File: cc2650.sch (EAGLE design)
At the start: 27 parts, among them IC1 TPS73133DBVR, IC4 CC2650MODAMOHR, SW1 SPST_TACT-KMR2, SW3 SPST_TACT-KMR2

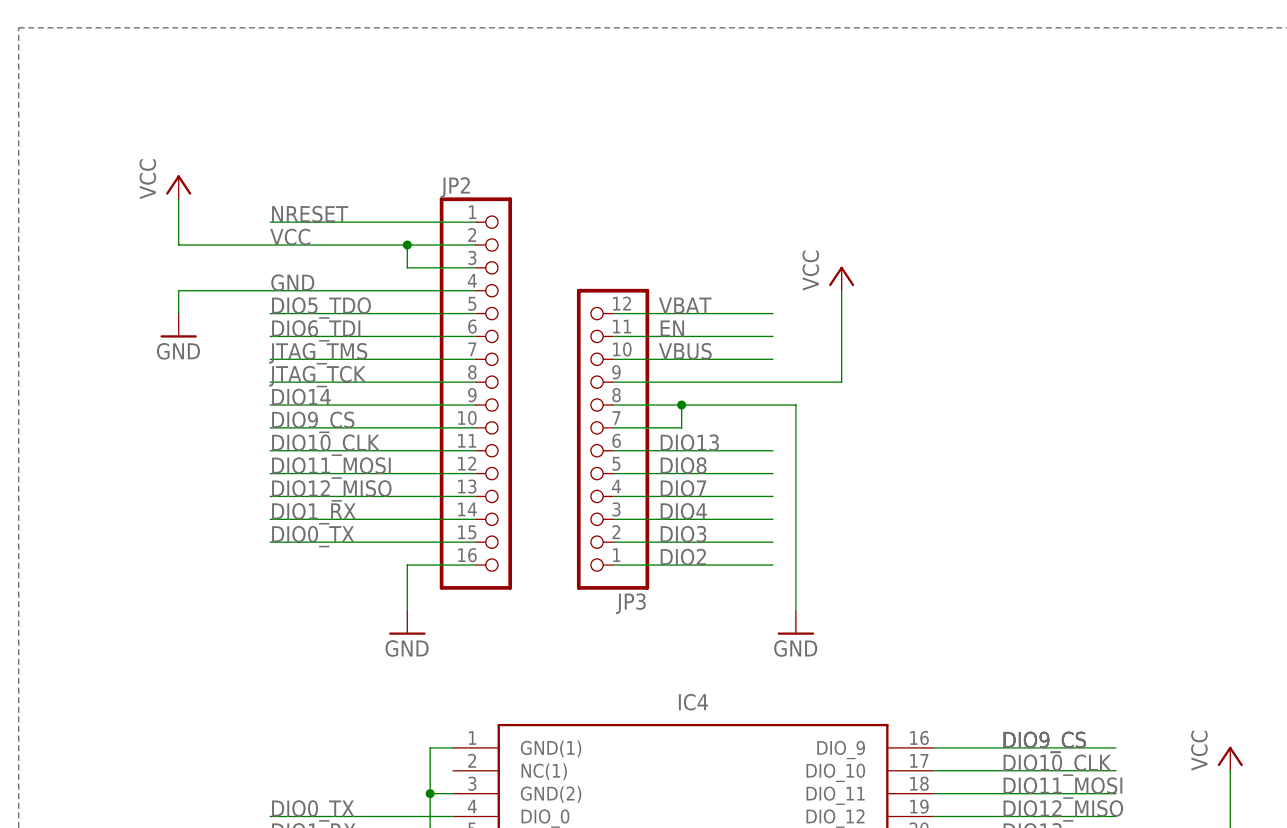
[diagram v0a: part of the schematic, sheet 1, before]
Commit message: modified adafruit FeatehrWing pin part to remove bottom left hole. Swapped modified FeatherWing for the 1x12 & 1x16 pin headers.
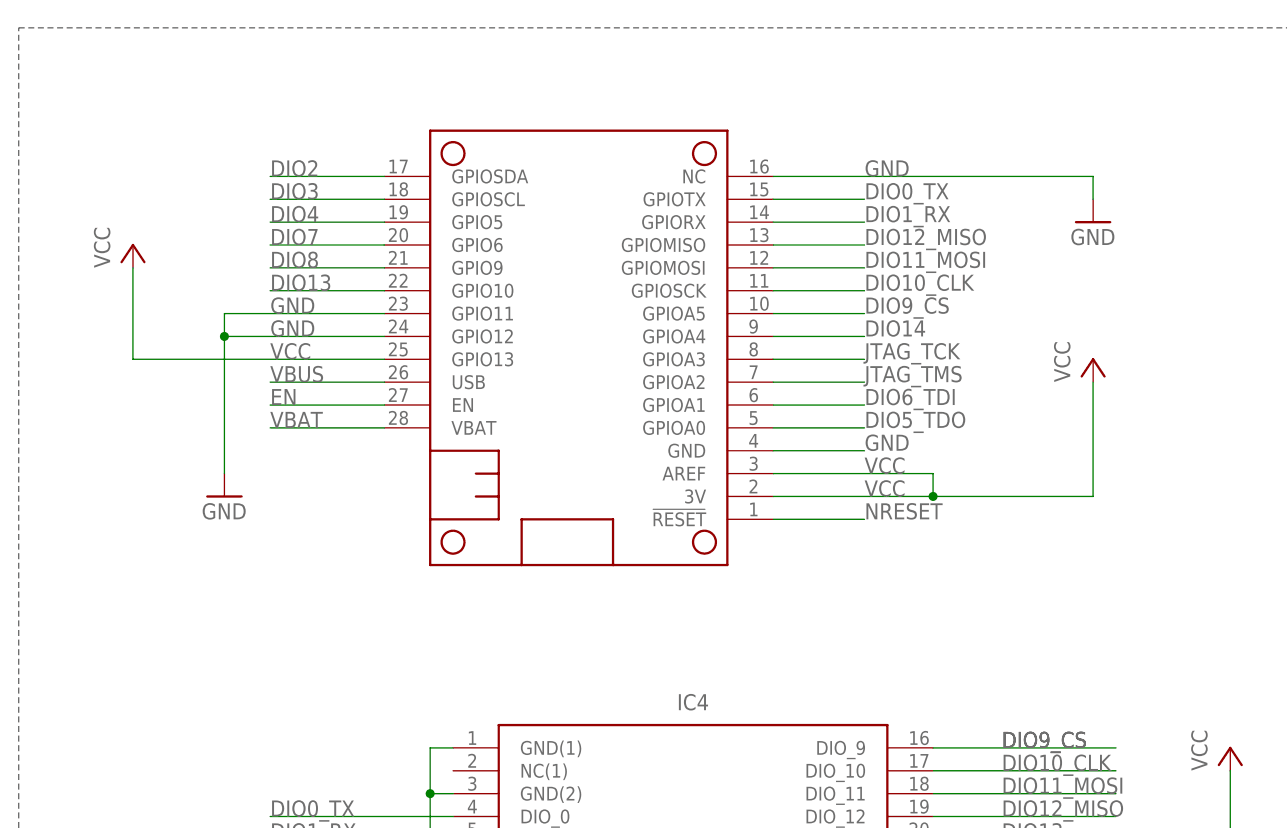
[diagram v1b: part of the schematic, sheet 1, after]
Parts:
- removed JP2: (no value), microbuilder:HEADER-1X16ROUND
- removed JP3: (no value), microbuilder:HEADER-1X12
- added MS1: FEATHERWING_NODIM, wing_modified:FEATHERWING_NODIM
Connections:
- net DIO0_TX: now also MS1.GPIOTX; no longer JP2.15
- net DIO10_CLK: now also MS1.GPIOSCK; no longer JP2.11
- net DIO11_MOSI: now also MS1.GPIOMOSI; no longer JP2.12
- net DIO12_MISO: now also MS1.GPIOMISO; no longer JP2.13
- net DIO13: now also MS1.GPIO10; no longer JP3.6
- net DIO14: now also MS1.GPIOA4; no longer JP2.9
- net DIO1_RX: now also MS1.GPIORX; no longer JP2.14
- net DIO2: now also MS1.GPIOSDA; no longer JP3.1
- net DIO3: now also MS1.GPIOSCL; no longer JP3.2
- net DIO4: now also MS1.GPIO5; no longer JP3.3
- net DIO5_TDO: now also MS1.GPIOA0; no longer JP2.5
- net DIO6_TDI: now also MS1.GPIOA1; no longer JP2.6
- net DIO7: now also MS1.GPIO6; no longer JP3.4
- net DIO8: now also MS1.GPIO9; no longer JP3.5
- net DIO9_CS: now also MS1.GPIOA5; no longer JP2.10
- net EN: now also MS1.EN; no longer JP3.11
- net GND: now also MS1.GND, MS1.GPIO11, MS1.GPIO12, MS1.NC; no longer JP2.16, JP2.4, JP3.7, JP3.8
- net JTAG_TCK: now also MS1.GPIOA3; no longer JP2.8
- net JTAG_TMS: now also MS1.GPIOA2; no longer JP2.7
- net NRESET: now also MS1.!RESET; no longer JP2.1
- net VBAT: now also MS1.VBAT; no longer JP3.12
- net VBUS: now also MS1.USB; no longer JP3.10
- net VCC: now also MS1.3V, MS1.AREF, MS1.GPIO13; no longer JP2.2, JP2.3, JP3.9
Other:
- note removed: "Mounting Holes: 125 mil for 4-40/M2.5/M3 screws"

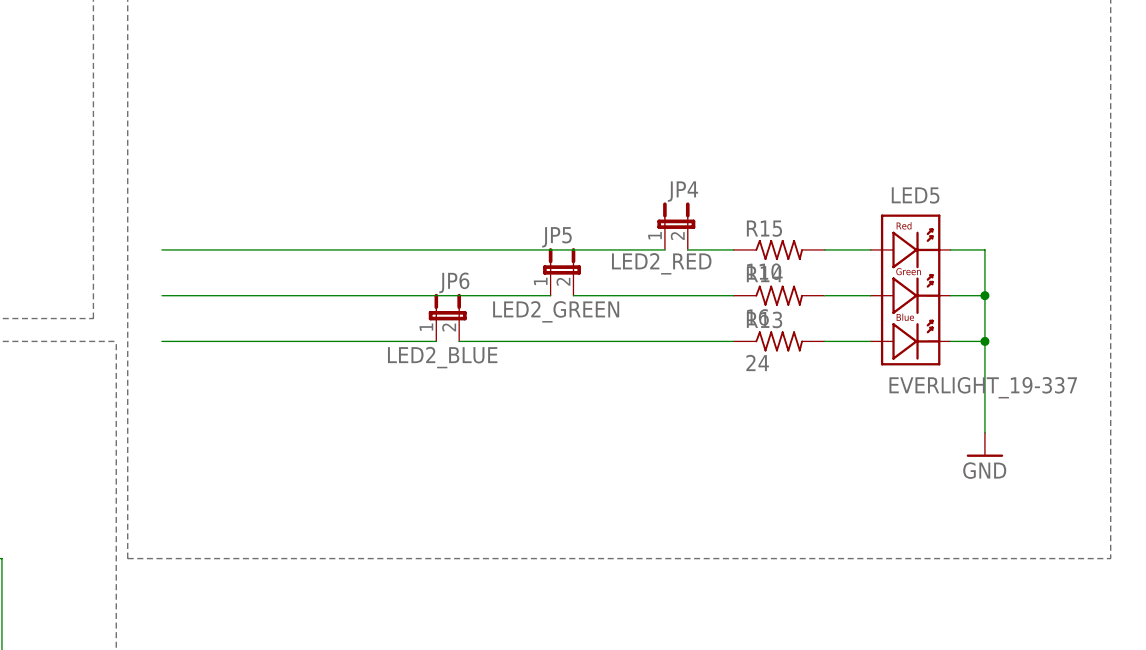
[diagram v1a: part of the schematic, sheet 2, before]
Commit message: removed RGB LED. Removed extra power pins from pin headers.
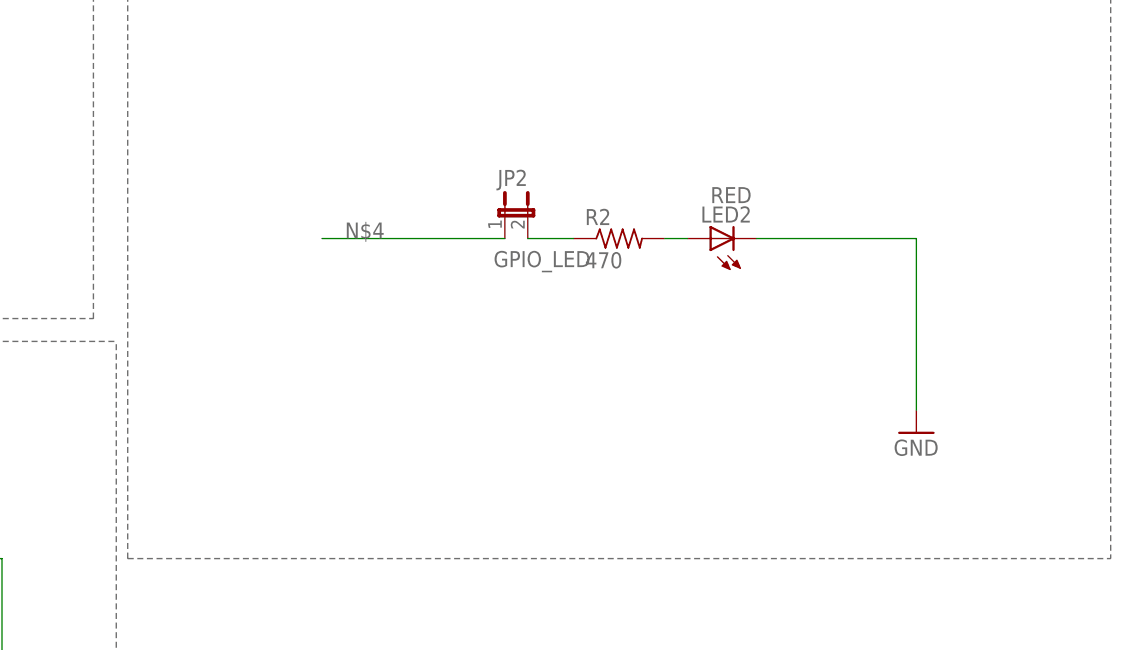
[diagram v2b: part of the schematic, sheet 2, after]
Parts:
- removed JP4: LED2_RED, jumper:JP1M
- removed JP5: LED2_GREEN, jumper:JP1M
- removed JP6: LED2_BLUE, jumper:JP1M
- removed LED5: EVERLIGHT_19-337, MSP-EXP432:EVERLIGHT_19-337
- removed R13: 24, adafruit:R-US_R1206
- removed R14: 16, adafruit:R-US_R1206
- removed R15: 110, adafruit:R-US_R1206
- added JP2: GPIO_LED, jumper:JP1M
- added LED2: RED, adafruit:LEDCHIPLED_1206
- added R2: 470, adafruit:R-US_R1206
- JP1: value LED1 -> PWR_LED
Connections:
- removed net N$12: JP6.2, R13.1
- removed net N$5: LED5.GA, R14.2
- removed net N$6: LED5.BA, R13.2
- removed net N$7: JP5.2, R14.1
- removed net P2.0_RGBLED_RED: JP4.1
- removed net P2.1_RGBLED_GREEN: JP5.1
- removed net P2.2_RGBLED_BLUE: JP6.1
- new net N$2: LED2.A, R2.2
- net GND: now also LED2.C; no longer LED5.BC, LED5.GC, LED5.RC, MS1.GPIO11, MS1.GPIO12
- net N$3: now also JP2.2, R2.1; no longer JP4.2, R15.1
- net N$4: now also JP2.1; no longer LED5.RA, R15.2
- net VCC: no longer MS1.AREF, MS1.GPIO13

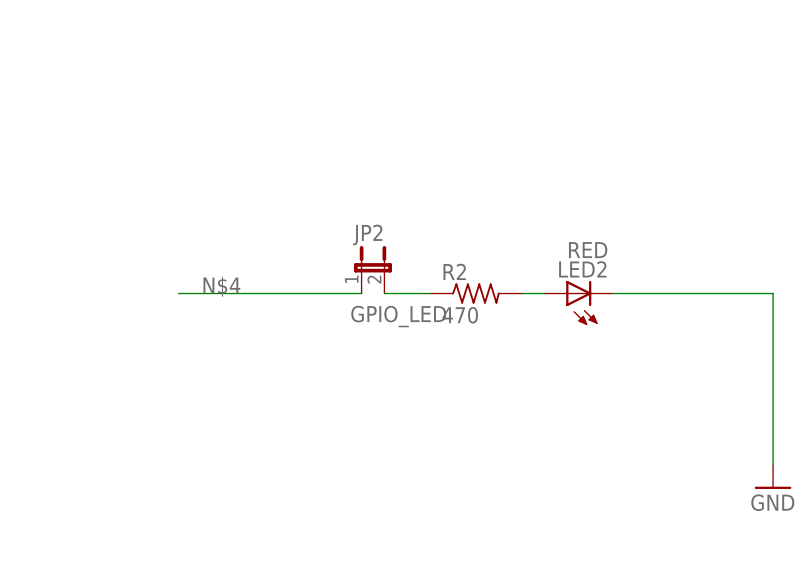
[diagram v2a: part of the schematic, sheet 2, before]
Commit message: changed resistor values for LEDS.
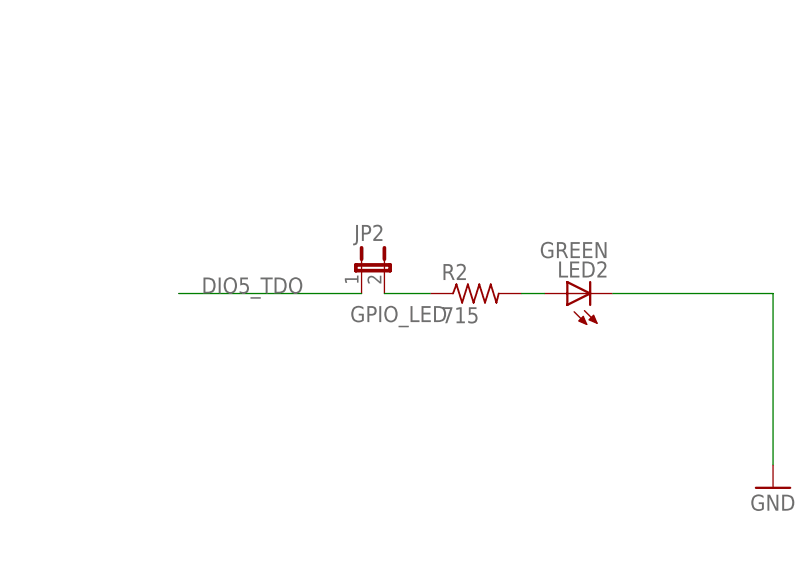
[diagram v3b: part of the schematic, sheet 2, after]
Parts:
- LED2: value RED -> GREEN
- R2: value 470 -> 715
- R3: value 470 -> 787
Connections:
- removed net N$4: JP2.1
- net DIO5_TDO: now also JP2.1
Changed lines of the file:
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@@
 <attribute name="OC_NEWARK" value="10N9702"/>
 </part>
-<part name="R3" library="adafruit" deviceset="R-US_" device="R1206" value="470">
+<part name="R3" library="adafruit" deviceset="R-US_" device="R1206" value="787">
 <attribute name="MF" value=""/>
 <attribute name="MPN" value="CR1206-FX-4700ELF"/>
@@
 <part name="GND5" library="supply1" library_urn="urn:adsk.eagle:library:371" deviceset="GND" device=""/>
 <part name="P+2" library="supply1" library_urn="urn:adsk.eagle:library:371" deviceset="VCC" device=""/>
-<part name="R2" library="adafruit" deviceset="R-US_" device="R1206" value="470">
+<part name="R2" library="adafruit" deviceset="R-US_" device="R1206" value="715">
 <attribute name="MF" value=""/>
 <attribute name="MPN" value="CR1206-FX-4700ELF"/>
 <attribute name="OC_NEWARK" value="06X5194"/>
 </part>
-<part name="LED2" library="adafruit" deviceset="LED" device="CHIPLED_1206" value="RED">
+<part name="LED2" library="adafruit" deviceset="LED" device="CHIPLED_1206" value="GREEN">
 <attribute name="MF" value=""/>
 <attribute name="MPN" value="HSMC-C150"/>
@@
 </segment>
 </net>
-<net name="N$4" class="0">
+<net name="DIO5_TDO" class="0">
 <segment>
 <pinref part="JP2" gate="G$1" pin="1"/>

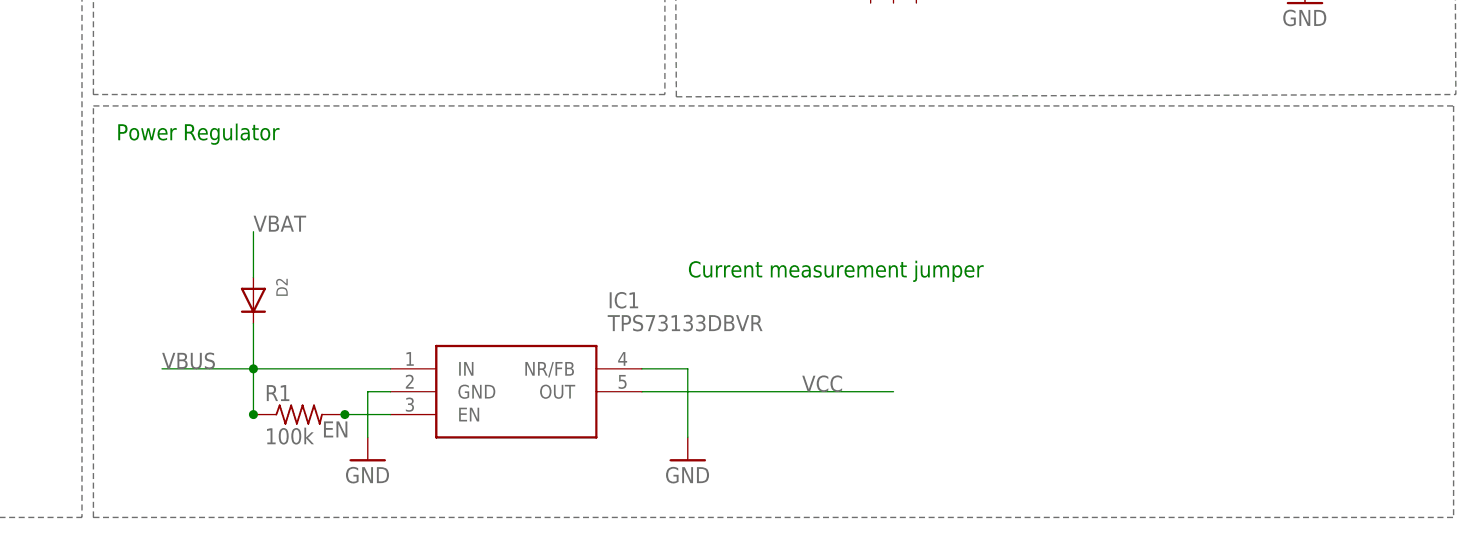
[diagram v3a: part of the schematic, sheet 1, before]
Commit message: changed power circuitry
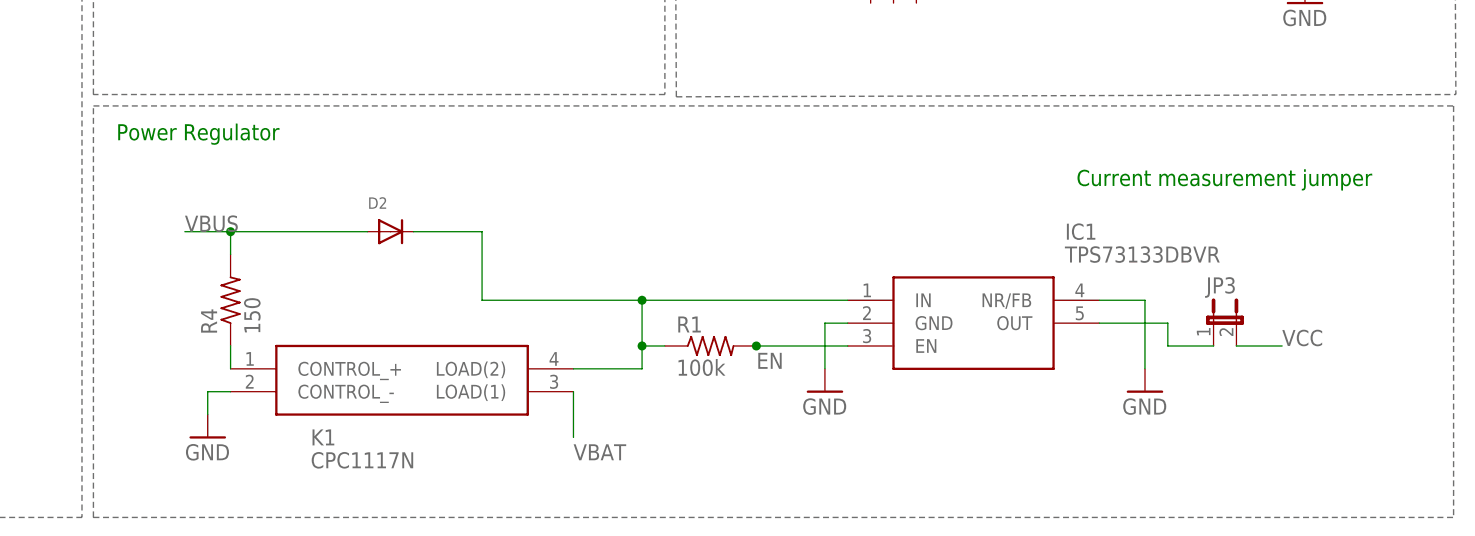
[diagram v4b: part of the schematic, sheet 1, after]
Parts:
- added JP3: PWR_LED, jumper:JP1M
- added K1: CPC1117N, CPC1117N:CPC1117N
- added R4: 150, adafruit:R-US_R1206
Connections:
- new net N$4: D2.C, IC1.IN, K1.LOAD(2), R1.1
- new net N$5: IC1.OUT, JP3.1
- new net N$6: K1.CONTROL_+, R4.1
- net GND: now also K1.CONTROL_-
- net VBAT: now also K1.LOAD(1); no longer D2.A
- net VBUS: now also D2.A, R4.2; no longer D2.C, IC1.IN, R1.1
- net VCC: now also JP3.2; no longer IC1.OUT
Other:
- moved on the sheet: D2, IC1, R1
